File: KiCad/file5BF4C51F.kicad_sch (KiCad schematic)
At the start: 7 parts, among them J401 CONN_01X06, J402 CONN_01X10, J403 CONN_01X10

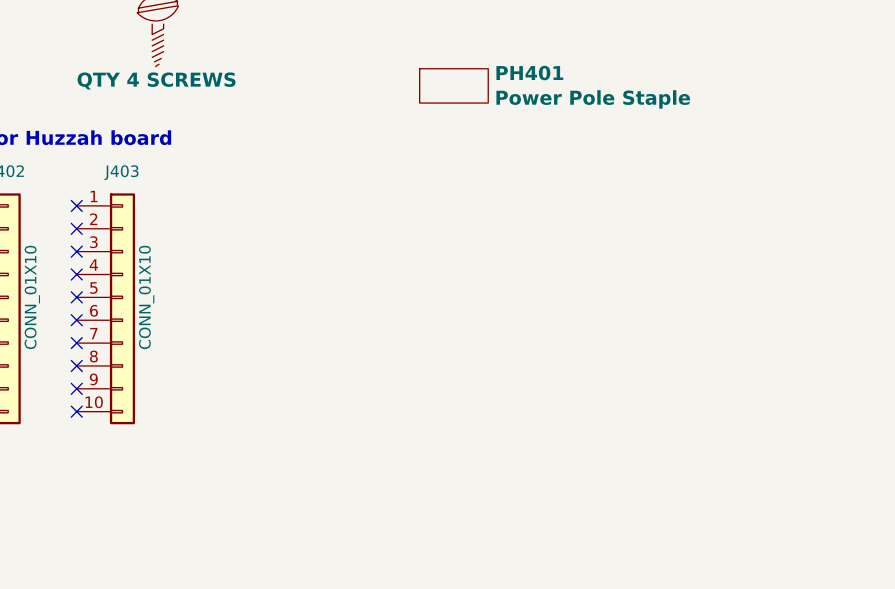
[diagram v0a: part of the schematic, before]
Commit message: KiCad Updates
o Fixes for problems found during first board build
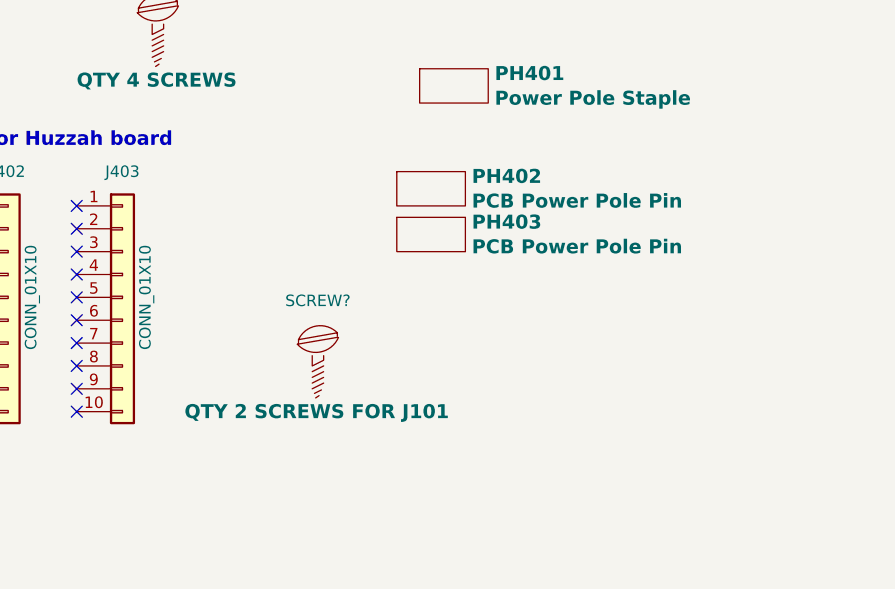
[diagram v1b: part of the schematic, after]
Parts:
- added PH402, PH403: PCB Power Pole Pin, Oddities:Dummy_Empty, symbol FlexFox80-rescue:PinlessHardware-Device
- added SCREW?: QTY 2 SCREWS FOR J101, Oddities:Dummy_Empty, symbol special:SCREW
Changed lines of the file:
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@@
       (effects (font (size 1.524 1.524)) hide)
+    )
+    (property "Description" "PCB retaining screws" (id 6) (at 111.76 67.31 0)
+      (effects (font (size 1.27 1.27)) hide)
     )
   )
@@
     (pin "9")
   )
+  (symbol (lib_id "special:SCREW") (at 129.54 104.14 0) (unit 1)
+    (in_bom yes) (on_board yes)
+    (property "Reference" "SCREW?" (id 0) (at 129.667 96.901 0))
+    (property "Value" "QTY 2 SCREWS FOR J101" (id 1) (at 129.54 109.22 0)
+      (effects (font (size 1.5494 1.5494) bold))
+    )
+    (property "Footprint" "Oddities:Dummy_Empty" (id 2) (at 129.667 104.14 0)
+      (effects (font (size 1.27 1.27)) hide)
+    )
+    (property "Datasheet" "" (id 3) (at 129.667 104.14 0))
+    (property "Part No." "" (id 4) (at 129.54 104.14 0)
+      (effects (font (size 1.524 1.524)) hide)
+    )
+    (property "Description" "2mm x 0.4mm x 6mm Phillips pan head" (id 5) (at 129.54 104.14 0)
+      (effects (font (size 1.27 1.27)) hide)
+    )
+  )
+  (symbol (lib_id "FlexFox80-rescue:PinlessHardware-Device") (at 142.24 87.63 0) (unit 1)
+    (in_bom yes) (on_board yes)
+    (property "Reference" "PH402" (id 0) (at 146.7612 83.0834 0)
+      (effects (font (size 1.5494 1.5494) bold) (justify left))
+    )
+    (property "Value" "PCB Power Pole Pin" (id 1) (at 146.7612 85.8266 0)
+      (effects (font (size 1.5494 1.5494) bold) (justify left))
+    )
+    (property "Footprint" "Oddities:Dummy_Empty" (id 2) (at 142.24 87.63 0)
+      (effects (font (size 0.9906 0.9906)) hide)
+    )
+    (property "Datasheet" "" (id 3) (at 142.24 87.63 0)
+      (effects (font (size 0.9906 0.9906)) hide)
+    )
+    (property "Part No." "2243-114555P2-ND" (id 4) (at 142.24 87.63 0)
+      (effects (font (size 1.27 1.27)) hide)
+    )
+    (property "Link" "<a href=\"https://www.digikey.com/products/en?keywords=2243-1377G2-BK-ND\">Link</a>" (id 5) (at 142.24 87.63 0)
+      (effects (font (size 1.27 1.27)) hide)
+    )
+    (property "Manufacturer" "Anderson Power Products, Inc." (id 6) (at 142.24 87.63 0)
+      (effects (font (size 1.27 1.27)) hide)
+    )
+    (property "Manufacturer PN" "1377G2-BK" (id 7) (at 142.24 87.63 0)
+      (effects (font (size 1.27 1.27)) hide)
+    )
+    (property "Description" "RIGHT ANGLE PCB CONT .40/1.295 B" (id 8) (at 142.24 87.63 0)
+      (effects (font (size 1.27 1.27)) hide)
+    )
+    (property "Digi-Key Part No." "2243-1377G2-BK-ND" (id 9) (at 142.24 87.63 0)
+      (effects (font (size 1.27 1.27)) hide)
+    )
+  )
+  (symbol (lib_id "FlexFox80-rescue:PinlessHardware-Device") (at 142.24 92.71 0) (unit 1)
+    (in_bom yes) (on_board yes)
+    (property "Reference" "PH403" (id 0) (at 146.7612 88.1634 0)
+      (effects (font (size 1.5494 1.5494) bold) (justify left))
+    )
+    (property "Value" "PCB Power Pole Pin" (id 1) (at 146.7612 90.9066 0)
+      (effects (font (size 1.5494 1.5494) bold) (justify left))
+    )
+    (property "Footprint" "Oddities:Dummy_Empty" (id 2) (at 142.24 92.71 0)
+      (effects (font (size 0.9906 0.9906)) hide)
+    )
+    (property "Datasheet" "" (id 3) (at 142.24 92.71 0)
+      (effects (font (size 0.9906 0.9906)) hide)
+    )
+    (property "Part No." "2243-114555P2-ND" (id 4) (at 142.24 92.71 0)
+      (effects (font (size 1.27 1.27)) hide)
+    )
+    (property "Link" "<a href=\"https://www.digikey.com/products/en?keywords=2243-1377G2-BK-ND\">Link</a>" (id 5) (at 142.24 92.71 0)
+      (effects (font (size 1.27 1.27)) hide)
+    )
+    (property "Manufacturer" "Anderson Power Products, Inc." (id 6) (at 142.24 92.71 0)
+      (effects (font (size 1.27 1.27)) hide)
+    )
+    (property "Manufacturer PN" "1377G2-BK" (id 7) (at 142.24 92.71 0)
+      (effects (font (size 1.27 1.27)) hide)
+    )
+    (property "Description" "RIGHT ANGLE PCB CONT .40/1.295 B" (id 8) (at 142.24 92.71 0)
+      (effects (font (size 1.27 1.27)) hide)
+    )
+    (property "Digi-Key Part No." "2243-1377G2-BK-ND" (id 9) (at 142.24 92.71 0)
+      (effects (font (size 1.27 1.27)) hide)
+    )
+  )
 )
